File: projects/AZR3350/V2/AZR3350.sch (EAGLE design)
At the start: 168 parts, among them IC1 LM2734Y, IC11 74HC125, IC2 LDO-TS1117CW-3V3, IC3 74S08D, IC5 A4988, IC6 A4988, IC7 A4988, IC8 A4988, IC9 SI87XXIS, J107 ZX62-AB-5PA, Q1 FDS6890A, Q2 IRF520, Q3 IRF520, X3 MSTBV4

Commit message: Found all of the parts on DigiKey
(and replaced most that didn't work, for various reasons)
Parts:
- removed IC11: 74HC125, misc:74HC125
- removed L6: 10uH 100MHz, Zero_V1.0:INDUCTOR-0603
- removed R75: 4K7, resistor:R-US_R0603
- removed R76: 180R, resistor:R-US_R0603
- removed U$2: ATSAM4S8C, misc:ATSAM4S8C
- removed U$3: MICROSD, adafruit:MICROSD
- added 5V, USB: (no value), led:LEDCHIPLED_0805
- added C37, C38, C39, C41: 100n, resistor:C-EUC0603
- added C40, C42: 220n, resistor:C-EUC0603
- added F1: MC36207, misc:MC36207
- added IC10: A4988, RepRapjr:A4988
- added IC4: SI87XXIS, misc:SI87XXIS
- added J4: MOLEX-105162-001, misc:MOLEX-105162-001
- added J_ERASE: (no value), jumper:JP1Q
- added L3: 10uH 100MHz, Zero_V1.0:INDUCTOR-0603
- added Q4: BUK9Y53-100B, misc:BUK9Y53-100B
- added R62, R69: 100K, resistor:R-US_R0603
- added R63, R70: 10K, resistor:R-TRIMM3103
- added R64, R71: 20K, resistor:R-US_R0603
- added R65, R67: 10K, resistor:R-US_R0603
- added R66, R68: 0R2, resistor:R-US_R0805
- added RESET: PUSHBUTTON3, Zero_V1.0:PUSHBUTTON3
- added X1: 12MHz, misc:CRYSTAL-4PIN
- C1: value 10uF -> 10n; device resistor:CPOL-USD -> resistor:C-EUC0603
- C11, C16, C23: value 220n -> 100n
- C13, C20: value 100u -> 100n; device resistor:CPOL-USD -> resistor:C-EUC0603
- C15, C36: value 100n -> 2.2u
- C18, C32: value 220n -> 10u
- C19: value 100n -> 4u7
- C2: value 10n -> 10uF; device resistor:C-EUC0603 -> resistor:CPOL-USD
- C25, C9: value 220n -> 10u; device resistor:C-EUC0603 -> resistor:C-EUC0805
- C27: value 100u -> 2.2u 0.1-10ohm ESR; device resistor:CPOL-USD -> resistor:C-EUC0603
- C28: value 100n -> 10n
- C29: value 100n -> 10p
- C3: value 47u -> 100n; device resistor:CPOL-USD -> resistor:C-EUC0603
- C30: value 220n -> 10p
- C31: value 100n -> 10u
- C33: value 100n -> 2K2
- C34: value 100u -> 2.2u; device resistor:CPOL-USD -> resistor:C-EUC0603
- C4: value 4.7uF -> 47u; device resistor:C-EUC0603 -> resistor:CPOL-USD
- C43: value 2.2u -> 100n
- C44: value 2.2u -> 100u; device resistor:C-EUC0603 -> resistor:CPOL-USD
- C45, C46, C53, C55: value 10u -> 100n
- C47: value 2K2 -> 220n
- C49, C54, C56, C61, C63: value 100n -> 220n
- C5: value 10uF -> 4.7uF; device resistor:CPOL-USD -> resistor:C-EUC0603
- C51, C58: value 100n -> 100u; device resistor:C-EUC0603 -> resistor:CPOL-USD
- C57: value 4u7 -> 100n
- C6: value 4.7uF -> 10uF; device resistor:C-EUC0603 -> resistor:CPOL-USD
- C60: value 2.2u 0.1-10ohm ESR -> 100n
- C65: value 10u -> 100u; device resistor:C-EUC0603 -> resistor:CPOL-USD
- C7: value 100n -> 4.7uF
- D1: device Diodi:0012_CD1206-S01575 -> adafruit:DIODE_SOD-123FL
- D2: device Diodi:0012_CD1206-S01575 -> diode:DIODE-SOD123
- IC3: value 74S08D -> ATSAM4S8C; device 74xx-us:74S08D -> misc:ATSAM4S8C
- IC5: value A4988 -> 74HC125; device RepRapjr:A4988 -> misc:74HC125
- IC6: value A4988 -> 74S08D; device RepRapjr:A4988 -> 74xx-us:74S08D
- IC9: value SI87XXIS -> A4988; device misc:SI87XXIS -> RepRapjr:A4988
- Q1: value FDS6890A -> NX138BKS; device transistor-power:FDS6890A -> misc:NX138BKS
- R1: value 10k -> 47K
- R10: value 47R -> 27K
- R11: value 10K -> 47K
- R12, R14, R33: value 0R2 -> 10K; device resistor:R-US_R0805 -> resistor:R-US_R0603
- R13: value 10K -> 1R
- R15: value 100K -> 4K7
- R16: value 10K -> 470R; device resistor:R-TRIMM3103 -> resistor:R-US_R0603
- R17: value 20K -> 47R
- R18: value 10K -> 47R
- R19: value 0R2 -> 47R; device resistor:R-US_R0805 -> resistor:R-US_R0603
- R2: value 52.3k -> 4K7
- R20: value 10K -> 2K2
- R21: value 0R2 -> 2K2; device resistor:R-US_R0805 -> resistor:R-US_R0603
- R22: value 100K -> 470R
- R23: value 10K -> 2K2; device resistor:R-TRIMM3103 -> resistor:R-US_R0603
- R24: value 20K -> 2K2
- R25, R27: value 10K -> 220R
- R26: value 0R2 -> 220R; device resistor:R-US_R0805 -> resistor:R-US_R0603
- R28: value 0R2 -> 100R; device resistor:R-US_R0805 -> resistor:R-US_R0603
- R29: value 100K -> 220R
- R3: value 10k -> 100k
- R30: value 10K -> 220R; device resistor:R-TRIMM3103 -> resistor:R-US_R0603
- R31: value 20K -> 220R
- R34: value 10K -> 1K
- R35: value 0R2 -> 1K; device resistor:R-US_R0805 -> resistor:R-US_R0603
- R36: value 100K -> 180R
- R37: value 10K -> 180R; device resistor:R-TRIMM3103 -> resistor:R-US_R0603
- R38: value 20K -> 10K
- R39: value 4K7 0.1% -> 10K
- R4: value 10K -> 5.53k
- R40: value 47R -> 4K7 0.1%
- R41: value 2K2 -> 4K7 0.1%
- R42, R43: value 1K -> 4K7
- R44: value 180R -> 10K
- R45: value 180R -> 0R2; device resistor:R-US_R0603 -> resistor:R-US_R0805
- R46, R51: value 4K7 -> 10K
- R47: value 4K7 -> 0R2; device resistor:R-US_R0603 -> resistor:R-US_R0805
- R48: value 470R -> 100K
- R49: value 2K2 -> 10K; device resistor:R-US_R0603 -> resistor:R-TRIMM3103
- R5: value 10K -> 10k
- R50: value 2K2 -> 20K
- R52: value 220R -> 0R2; device resistor:R-US_R0603 -> resistor:R-US_R0805
- R53, R58: value 220R -> 10K
- R54: value 100R -> 0R2; device resistor:R-US_R0603 -> resistor:R-US_R0805
- R55: value 220R -> 100K
- R56: value 220R -> 10K; device resistor:R-US_R0603 -> resistor:R-TRIMM3103
- R57: value 220R -> 20K
- R59: value 10K -> 0R2; device resistor:R-US_R0603 -> resistor:R-US_R0805
- R6: value 4K7 0.1% -> 4K7
- R61: value 1R -> 0R2; device resistor:R-US_R0603 -> resistor:R-US_R0805
- R7: value 470R -> 2K2
- R8: value 2K2 -> 180R
- R9: value 47R -> 2K2
- renumbered D103 to D4, J107 to J1, X3 to J3
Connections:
- removed net EN: IC1.EN, R1.2
- removed net N$19: R58.2, R59.1, U$3.CARD_DETECT, U$3.CARD_DETECT1
- removed net N$33: R75.1, VIN.C
- removed net N$34: 3V3.C, R76.1
- new net 24V_LED: R6.1, VIN.C
- new net 3V3_LED: 3V3.C, R8.1
- new net 5V_LED: 5V.C, R7.1
- new net CARDDETECT: J4.CARD_DETECT, R25.2, R32.1
- new net ERASE: IC3.ERASE/PB12, J_ERASE.2
- new net PWR_FAIL_DET: C1.1, IC3.PC12/AD12, R1.1, R2.2
- new net SHDN: IC1.EN, R3.2
- new net USB_LED: R9.1, USB.C
- new net USB_PWR_MON: C8.2, IC3.PC11, R10.2, R11.1
- new net VSSA: C15.1, F1.1, R12.2, T_BED-2.S, T_EXT-2.S
- new net VSSA_MON: IC3.PA17/PGMD5/AD0, R12.1
- new net XIN: C29.1, IC3.PB9/PGMCK/XIN, X1.3
- new net XOUT: C30.1, IC3.PB8/XOUT, X1.1
- net +24V: now also C2.+, C39.2, C41.1, C43.1, C44.+, C46.2, C48.1, C50.1, C51.+, C53.2, C55.1, C57.1, C58.+, C60.2, C62.1, C64.1, C65.+, IC10.VBB1, IC10.VBB2, IC9.VBB1, IC9.VBB2, R3.1, R42.2; no longer C1.+, C10.1, C12.1, C13.+, C15.2, C17.1, C19.1, C20.+, C22.2, C24.1, C26.1, C27.+, C29.2, C31.1, C33.1, C34.+, C8.2, IC5.VBB1, IC5.VBB2, IC6.VBB1, IC6.VBB2, R1.1, R46.2
- net +3V3: now also C10.2, C11.2, C12.2, C13.2, C14.2, C16.1, C31.1, C33.1, C36.1, C42.1, C49.1, C56.1, C6.+, C63.1, C7.2, C9.2, IC10.MS1, IC10.MS2, IC10.MS3, IC10.VDD, IC3.VDDIN, IC3.VDDIO-27, IC3.VDDIO-50, IC3.VDDIO-69, IC3.VDDIO-91, IC3.VDDIO-98, IC4.VDD, IC5P.VCC, IC9.MS1, IC9.MS2, IC9.MS3, J4.VDD, J_ERASE.1, L3.2, R14.2, R32.2, R33.2, R46.2, R48.2, R50.2, R53.2, R55.2, R57.2, R62.2, R64.2, R67.2, R69.2, R71.2; no longer C11.1, C25.1, C35.1, C45.1, C46.1, C47.1, C48.2, C49.2, C5.+, C50.2, C51.2, C52.2, C53.2, C54.1, C55.1, C6.2, IC11P.VCC, IC5.MS1, IC5.MS2, IC5.MS3, IC5.VDD, IC6.MS1, IC6.MS2, IC6.MS3, IC6.VDD, L4.2, R13.2, R15.2, R17.2, R20.2, R22.2, R24.2, R27.2, R29.2, R31.2, R34.2, R36.2, R38.2, R59.2, U$2.VDDIN, U$2.VDDIO-27, U$2.VDDIO-50, U$2.VDDIO-69, U$2.VDDIO-91, U$2.VDDIO-98, U$3.VDD
- net +5V: now also 5V.A, C37.1, C4.+, C5.1, EXP_2-10.S, IC6P.VCC, R4.1; no longer C3.+, C36.1, C4.1, EXP_1-10.S, IC3P.VCC, R2.1
- net ADVREF: now also C17.1, IC3.ADVREF, L3.1, R40.2, R41.2; no longer C56.1, L4.1, R39.2, R6.2, U$2.ADVREF
- net BED: now also IC3.PA15/PGMD3, R37.1; no longer R45.1, U$2.PA15/PGMD3
- net BEEPER: now also EXP_2-1.S, IC3.PC22; no longer EXP_1-1.S, U$2.PC22
- net BOOST: now also C3.1; no longer C2.1
- net BTN_EN1: now also EXP_1-5.S, IC3.PC20; no longer EXP_2-5.S, U$2.PC20
- net BTN_EN2: now also EXP_1-3.S, IC3.TCK/SWCLK/PB7; no longer EXP_2-3.S, U$2.TCK/SWCLK/PB7
- net BTN_ENC: now also EXP_2-2.S, IC3.PC14; no longer EXP_1-2.S, U$2.PC14
- net CP1E: now also C59.1, IC10.CP1; no longer C28.1, IC8.CP1
- net CP1X: now also C38.1, IC7.CP1; no longer C7.1, IC5.CP1
- net CP1Y: now also C45.1, IC8.CP1; no longer C14.1, IC6.CP1
- net CP1Z: now also C52.1, IC9.CP1; no longer C21.1, IC7.CP1
- net CP2E: now also C59.2, IC10.CP2; no longer C28.2, IC8.CP2
- net CP2X: now also C38.2, IC7.CP2; no longer C7.2, IC5.CP2
- net CP2Y: now also C45.2, IC8.CP2; no longer C14.2, IC6.CP2
- net CP2Z: now also C52.2, IC9.CP2; no longer C21.2, IC7.CP2
- net EDR_CONN: now also R23.2; no longer R49.2
- net EMOT1A: now also IC10.OUT1A; no longer IC8.OUT1A
- net EMOT1B: now also IC10.OUT1B; no longer IC8.OUT1B
- net EMOT2A: now also IC10.OUT2A; no longer IC8.OUT2A
- net EMOT2B: now also IC10.OUT2B; no longer IC8.OUT2B
- net ESP_CS: now also R24.2; no longer R50.2
- net ESP_DATA_RDY: now also IC3.PC13/AD10, R23.1; no longer R49.1, U$2.PC13/AD10
- net ESP_EN: now also IC3.PA24/PGMD12, R15.1; no longer R51.1, U$2.PA24/PGMD12
- net ESP_MISO: now also R18.1; no longer R10.1
- net ESP_MOSI: now also R19.1; no longer R40.1
- net ESP_RESET: now also R16.2, R20.2; no longer R7.2, R8.2
- net ESP_RST: now also IC3.PC4, R16.1; no longer R7.1, U$2.PC4
- net ESP_SPCK: now also R17.1; no longer R9.1
- net ESP_URDX: now also R21.2; no longer R41.2
- net ESP_UTDX: now also R22.2; no longer R48.2
- net E_DIR: now also IC10.DIR, IC3.PC2; no longer IC8.DIR, U$2.PC2
- net E_EN: now also IC10.EN, IC3.PA8/XOUT32/PGMM0, R67.1; no longer IC8.EN, R34.1, U$2.PA8/XOUT32/PGMM0
- net E_STEP: now also IC10.STEP, IC3.PC1; no longer IC8.STEP, U$2.PC1
- net FAN1: now also IC3.PA18/PGMD6/AD1, R34.1; no longer R42.1, U$2.PA18/PGMD6/AD1
- net FAN2: now also IC3.PC26, R35.1; no longer R43.1, U$2.PC26
- net FB: now also R4.2, R5.1; no longer R2.2, R3.1
- net GND: now also C1.2, C10.1, C11.1, C12.1, C13.1, C14.1, C15.2, C2.-, C20.2, C21.2, C22.2, C27.2, C28.2, C29.2, C34.2, C37.2, C4.-, C40.2, C41.2, C42.2, C44.-, C48.2, C49.2, C5.2, C50.2, C51.-, C58.-, C6.-, C65.-, C7.1, C8.1, C9.1, F1.2, IC10.GND, IC10.GND1, IC10.NC, IC10.NC1, IC10.NC2, IC10.TH-PAD, IC3.GND-2, IC3.GND-26, IC3.GND-45, IC3.GND-70, IC3.GND-95, IC3.JTAGSEL, IC3.TST, IC4.C1, IC4.GND, IC5A.OE, IC5B.OE, IC5D.I, IC5D.OE, IC5P.GND, IC6A.I0, IC6A.I1, IC6P.GND, IC9.GND1, IC9.NC, IC9.NC1, IC9.NC2, IC9.TH-PAD, J4.GND, J4.VSS, R15.2, R2.1, R20.1, R44.2, R45.1, R47.1, R49.E, R5.2, R52.1, R54.1, R56.E, R58.2, R59.1, R6.2, R61.1, R63.E, R65.2, R66.1, R68.1, R7.2, R70.E, R8.2, R9.2, RESET.4, X1.2, X1.4; no longer C1.-, C10.2, C11.2, C12.2, C13.-, C20.-, C27.-, C3.-, C34.-, C4.2, C44.2, C45.2, C46.2, C48.1, C49.1, C5.-, C50.1, C51.1, C52.1, C53.1, C58.2, C59.2, C6.1, C60.2, C65.2, C9.2, IC11A.OE, IC11B.OE, IC11D.I, IC11D.OE, IC11P.GND, IC3A.I0, IC3A.I1, IC3P.GND, IC5.GND, IC5.GND1, IC5.NC, IC5.NC1, IC5.NC2, IC5.TH-PAD, IC6.GND, IC6.GND1, IC6.NC, IC6.NC1, IC6.NC2, IC6.TH-PAD, IC9.C1, R12.1, R14.1, R16.E, R18.2, R19.1, R21.1, R23.E, R25.2, R26.1, R28.1, R3.2, R30.E, R32.2, R33.1, R35.1, R37.E, R75.2, R76.2, R8.1, T_BED-2.S, T_EXT-2.S, U$2.GND-2, U$2.GND-26, U$2.GND-45, U$2.GND-70, U$2.GND-95, U$2.TST, U$3.GND, U$3.GND1, U$3.VSS
- net HOTEND: now also IC3.PC3, R36.1; no longer R44.1, U$2.PC3
- net LCD_CS: now also IC3.PC19, IC6B.I0, IC6B.I1, IC6C.I1, IC6D.I1; no longer IC3B.I0, IC3B.I1, IC3C.I1, IC3D.I1, U$2.PC19
- net LCD_CS_BUF: now also EXP_2-4.S, IC6B.O; no longer EXP_1-4.S, IC3B.O
- net LCD_MISO: now also IC3.PA5/PGMRDY, IC5C.O; no longer IC11C.O, U$2.PA5/PGMRDY
- net LCD_MISO_BUF: now also EXP_1-1.S, IC5C.I; no longer EXP_2-1.S, IC11C.I
- net LCD_MOSI: now also IC3.PB6/PGMNOE, IC5A.I, IC6C.I0; no longer IC11A.I, IC3C.I0, U$2.PB6/PGMNOE
- net LCD_MOSI_BUF: now also EXP_2-3.S, IC6C.O; no longer EXP_1-3.S, IC3C.O
- net LCD_RST: now also EXP_1-8.S, IC3.PC21; no longer EXP_2-8.S, U$2.PC21
- net LCD_SCK: now also IC3.PA2/PGMEN2, IC5B.I, IC6D.I0; no longer IC11B.I, IC3D.I0, U$2.PA2/PGMEN2
- net LCD_SCK_BUF: now also EXP_2-5.S, IC6D.O; no longer EXP_1-5.S, IC3D.O
- net LCD_SD_CS: now also EXP_1-4.S, IC3.PB13/DAC0, IC5C.OE; no longer EXP_2-4.S, IC11C.OE, U$2.PB13/DAC0
- net MCCDA: now also IC3.PA28, R27.1; no longer R53.1, U$2.PA28
- net MCCK: now also IC3.PA29, R28.1; no longer R54.1, U$2.PA29
- net MCDA0: now also IC3.PA30, R26.1; no longer R52.1, U$2.PA30
- net MCDA1: now also IC3.PA31, R30.1; no longer R56.1, U$2.PA31
- net MCDA2: now also IC3.PA26/PGMD14, R31.1; no longer R57.1, U$2.PA26/PGMD14
- net MCDA3: now also IC3.PA27/PGMD15, R29.1; no longer R55.1, U$2.PA27/PGMD15
- net MISO: now also IC3.PA12/PGMD0, R18.2; no longer R10.2, U$2.PA12/PGMD0
- net MOSI: now also IC3.PA13/PGMD1, R19.2; no longer R40.2, U$2.PA13/PGMD1
- net N$13: now also R34.2; no longer R42.2
- net N$18: now also R35.2; no longer R43.2
- net N$20: now also R36.2; no longer R44.2
- net N$25: now also R37.2; no longer R45.2
- net N$26: now also R42.1; no longer R46.1
- net N$27: now also R43.1; no longer R47.1
- net N$28: now also J4.DAT0, R26.2; no longer R52.2, U$3.DATA_OUT
- net N$29: now also J4.CMD, R27.2, R33.1; no longer R53.2, R60.1, U$3.DATA_IN
- net N$30: now also J4.CLK, R28.2; no longer R54.2, U$3.SCLK
- net N$31: now also J4.DAT3, R29.2; no longer R55.2, U$3.CS
- net N$32: now also J4.DAT1, R30.2; no longer R56.2, U$3.DAT1
- net N$35: now also J4.DAT2, R31.2; no longer R57.2, U$3.DAT2
- net N$37: now also C19.1, R13.1; no longer C57.1, R61.1
- net NPCS0: now also IC3.PA11/PGMM3, R24.1; no longer R50.1, U$2.PA11/PGMM3
- net NRST: now also C28.1, IC3.NRST, R14.1, RESET.2; no longer U$2.NRST
- net REFE: now also IC10.REF, R70.S; no longer IC8.REF, R37.S
- net REFE-IN: now also R70.A, R71.1; no longer R37.A, R38.1
- net REFX: now also IC7.REF, R49.S; no longer IC5.REF, R16.S
- net REFX-IN: now also R49.A, R50.1; no longer R16.A, R17.1
- net REFY: now also IC8.REF, R56.S; no longer IC6.REF, R23.S
- net REFY-IN: now also R56.A, R57.1; no longer R23.A, R24.1
- net REFZ: now also IC9.REF, R63.S; no longer IC7.REF, R30.S
- net REFZ-IN: now also R63.A, R64.1; no longer R30.A, R31.1
- net ROSCE: now also IC10.ROSC, R65.1; no longer IC8.ROSC, R32.1
- net ROSCX: now also IC7.ROSC, R44.1; no longer IC5.ROSC, R11.1
- net ROSCY: now also IC8.ROSC, R51.1; no longer IC6.ROSC, R18.1
- net ROSCZ: now also IC9.ROSC, R58.1; no longer IC7.ROSC, R25.1
- net RSTE: now also IC10.RST, IC10.SLP, R69.1; no longer IC8.RST, IC8.SLP, R36.1
- net RSTX: now also IC7.RST, IC7.SLP, R48.1; no longer IC5.RST, IC5.SLP, R15.1
- net RSTY: now also IC8.RST, IC8.SLP, R55.1; no longer IC6.RST, IC6.SLP, R22.1
- net RSTZ: now also IC9.RST, IC9.SLP, R62.1; no longer IC7.RST, IC7.SLP, R29.1
- net SAM_TFR_RDY: now also IC3.PA23/PGMD11; no longer U$2.PA23/PGMD11
- net SD_CD: now also IC3.PC8, R25.1; no longer R58.1, U$2.PC8
- net SD_MOSI_BUF: now also EXP_1-6.S, IC5A.O; no longer EXP_2-6.S, IC11A.O
- net SD_SCK_BUF: now also EXP_1-2.S, IC5B.O; no longer EXP_2-2.S, IC11B.O
- net SNS1E: now also IC10.SNS1, R66.2; no longer IC8.SNS1, R33.2
- net SNS1X: now also IC7.SNS1, R45.2; no longer IC5.SNS1, R12.2
- net SNS1Y: now also IC8.SNS1, R52.2; no longer IC6.SNS1, R19.2
- net SNS1Z: now also IC9.SNS1, R59.2; no longer IC7.SNS1, R26.2
- net SNS2E: now also IC10.SNS2, R68.2; no longer IC8.SNS2, R35.2
- net SNS2X: now also IC7.SNS2, R47.2; no longer IC5.SNS2, R14.2
- net SNS2Y: now also IC8.SNS2, R54.2; no longer IC6.SNS2, R21.2
- net SNS2Z: now also IC9.SNS2, R61.2; no longer IC7.SNS2, R28.2
- net SPCK: now also IC3.PA14/PGMD2, R17.2; no longer R9.2, U$2.PA14/PGMD2
- net SW: now also C3.2; no longer C2.2
- net T_BED: now also C35.1, IC3.PB1/AD5, R38.1; no longer C43.1, R4.1, U$2.PB1/AD5
- net T_BED_IN: now also R38.2, R41.1; no longer R4.2, R6.1
- net T_EXT: now also C34.1, IC3.PB0/AD4, R39.1; no longer C44.1, R5.1, U$2.PB0/AD4
- net T_EXT_IN: now also R39.2, R40.1; no longer R39.1, R5.2
- net URXD1: now also IC3.PB2/AD6, R21.1; no longer R41.1, U$2.PB2/AD6
- net USB_N: now also IC3.DDM/PB10; no longer U$2.DDM/PB10
- net USB_P: now also IC3.DDP/PB11; no longer U$2.DDP/PB11
- net UTXD1: now also IC3.PB3/AD7, R22.1; no longer R48.1, U$2.PB3/AD7
- net VBUS: now also R10.1, USB.A
- net VCPE: now also C60.1, IC10.VCP; no longer C29.1, IC8.VCP
- net VCPX: now also C39.1, IC7.VCP; no longer C8.1, IC5.VCP
- net VCPY: now also C46.1, IC8.VCP; no longer C15.1, IC6.VCP
- net VCPZ: now also C53.1, IC9.VCP; no longer C22.1, IC7.VCP
- net VDDOUT: now also C21.1, C22.1, C23.1, C24.1, C25.1, C26.1, C27.1, IC3.VDDCORE-16, IC3.VDDCORE-36, IC3.VDDCORE-56, IC3.VDDCORE-85, IC3.VDDOUT, L4.2; no longer C59.1, C60.1, C61.1, C62.1, C63.1, C64.1, C65.1, L6.2, U$2.VDDCORE-16, U$2.VDDCORE-36, U$2.VDDCORE-56, U$2.VDDCORE-85, U$2.VDDOUT
- net VDDPLL: now also C20.1, IC3.VDDPLL, L4.1, R13.2; no longer C58.1, L6.1, R61.2, U$2.VDDPLL
- net VIN: now also R1.2, R43.2; no longer R47.2
- net VREGE: now also C61.1, IC10.VREG; no longer C30.1, IC8.VREG
- net VREGX: now also C40.1, IC7.VREG; no longer C9.1, IC5.VREG
- net VREGY: now also C47.1, IC8.VREG; no longer C16.1, IC6.VREG
- net VREGZ: now also C54.1, IC9.VREG; no longer C23.1, IC7.VREG
- net XMOT1A: now also IC7.OUT1A; no longer IC5.OUT1A
- net XMOT1B: now also IC7.OUT1B; no longer IC5.OUT1B
- net XMOT2A: now also IC7.OUT2A; no longer IC5.OUT2A
- net XMOT2B: now also IC7.OUT2B; no longer IC5.OUT2B
- net X_DIR: now also IC3.PA1/PGMEN1, IC7.DIR; no longer IC5.DIR, U$2.PA1/PGMEN1
- net X_EN: now also IC3.PC17, IC7.EN, R46.1; no longer IC5.EN, R13.1, U$2.PC17
- net X_STEP: now also IC3.PC16, IC7.STEP; no longer IC5.STEP, U$2.PC16
- net X_STOP: now also IC3.TMS/SWDIO/PB6; no longer U$2.TMS/SWDIO/PB6
- net YMOT1A: now also IC8.OUT1A; no longer IC6.OUT1A
- net YMOT1B: now also IC8.OUT1B; no longer IC6.OUT1B
- net YMOT2A: now also IC8.OUT2A; no longer IC6.OUT2A
- net YMOT2B: now also IC8.OUT2B; no longer IC6.OUT2B
- net Y_DIR: now also IC3.PC9, IC8.DIR; no longer IC6.DIR, U$2.PC9
- net Y_EN: now also IC3.PA3, IC8.EN, R53.1; no longer IC6.EN, R20.1, U$2.PA3
- net Y_STEP: now also IC3.PC10, IC8.STEP; no longer IC6.STEP, U$2.PC10
- net Y_STOP: now also IC3.PC18; no longer U$2.PC18
- net ZMOT1A: now also IC9.OUT1A; no longer IC7.OUT1A
- net ZMOT1B: now also IC9.OUT1B; no longer IC7.OUT1B
- net ZMOT2A: now also IC9.OUT2A; no longer IC7.OUT2A
- net ZMOT2B: now also IC9.OUT2B; no longer IC7.OUT2B
- net Z_DIR: now also IC3.TDI/PB4, IC9.DIR; no longer IC7.DIR, U$2.TDI/PB4
- net Z_EN: now also IC3.PA4/PGMNCMD, IC9.EN, R60.1; no longer IC7.EN, R27.1, U$2.PA4/PGMNCMD
- net Z_STEP: now also IC3.PC28, IC9.STEP; no longer IC7.STEP, U$2.PC28
- net Z_STOP: now also IC3.TDO/TRACESWO/PB5, IC4.OUT; no longer IC9.OUT, U$2.TDO/TRACESWO/PB5
- net Z_STOP_IN: now also IC4.A1; no longer IC9.A1
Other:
- moved on the sheet: 3V3, C10, C11, C12, C14, C15, C16, C17, C18, C19, C21, C22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

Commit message: Changed out mosfets, other improvements (APSR)
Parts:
- removed Q4: BUK9Y53-100B, misc:BUK9Y53-100B
- Q2, Q3: value IRF520 -> BUK9Y53-100B; device transistor-power:IRF520 -> misc:BUK9Y53-100B
- RESET: value PUSHBUTTON3 -> (none); device Zero_V1.0:PUSHBUTTON3 -> misc:EVQQ2
- renumbered J_ERASE to ERASE
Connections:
- net CARDDETECT renamed DET
- net N$1 renamed VIN_F
- net N$10 renamed ESP_VIN
- net N$13 renamed FAN1_G
- net N$18 renamed FAN2_G
- net N$20 renamed EXT_G
- net N$21 renamed FAN2_D
- net N$22 renamed FAN1_D
- net N$23 renamed EXT_D
- net N$24 renamed BED_D
- net N$25 renamed BED_G
- net N$26 renamed EXT_L
- net N$27 renamed BED_L
- net N$28 renamed DAT0
- net N$29 renamed CMD
- net N$30 renamed CLK
- net N$31 renamed DAT3
- net N$32 renamed DAT1
- net N$35 renamed DAT2
- removed net NRST: C28.1, IC3.NRST, R14.1, RESET.2
- new net RESET: C28.1, IC3.NRST, R14.1, RESET.P1
- net GND: now also RESET.S, RESET.S1; no longer RESET.4

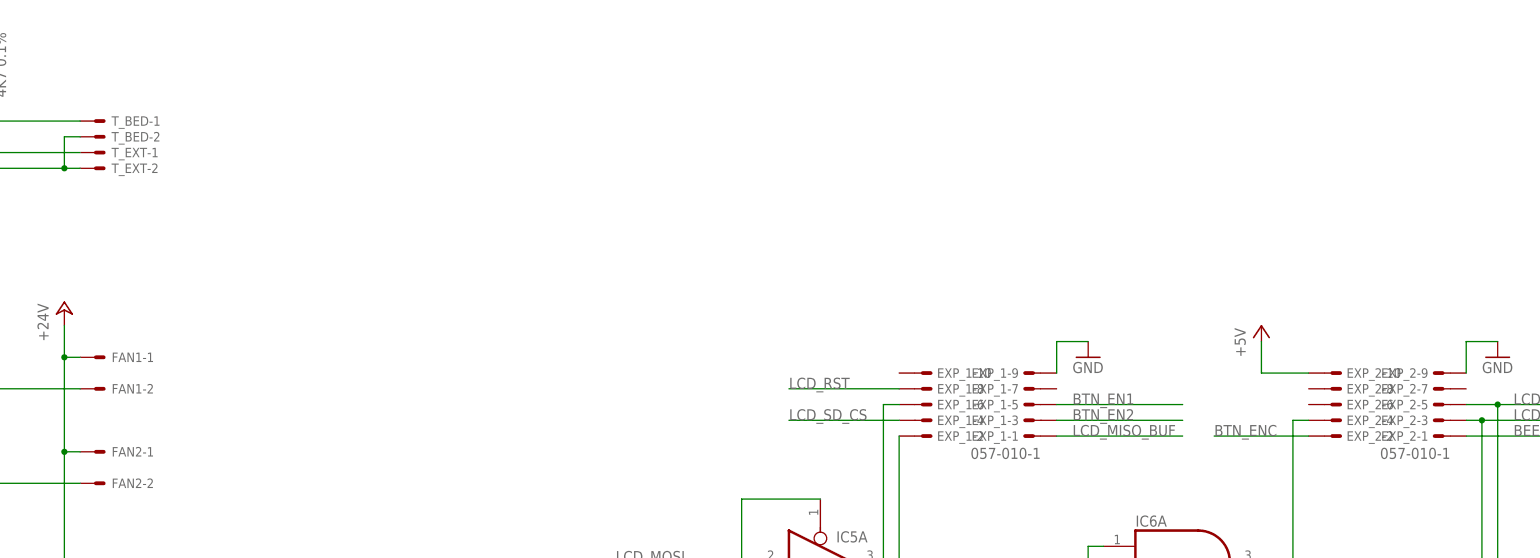
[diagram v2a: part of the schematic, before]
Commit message: LCD screen
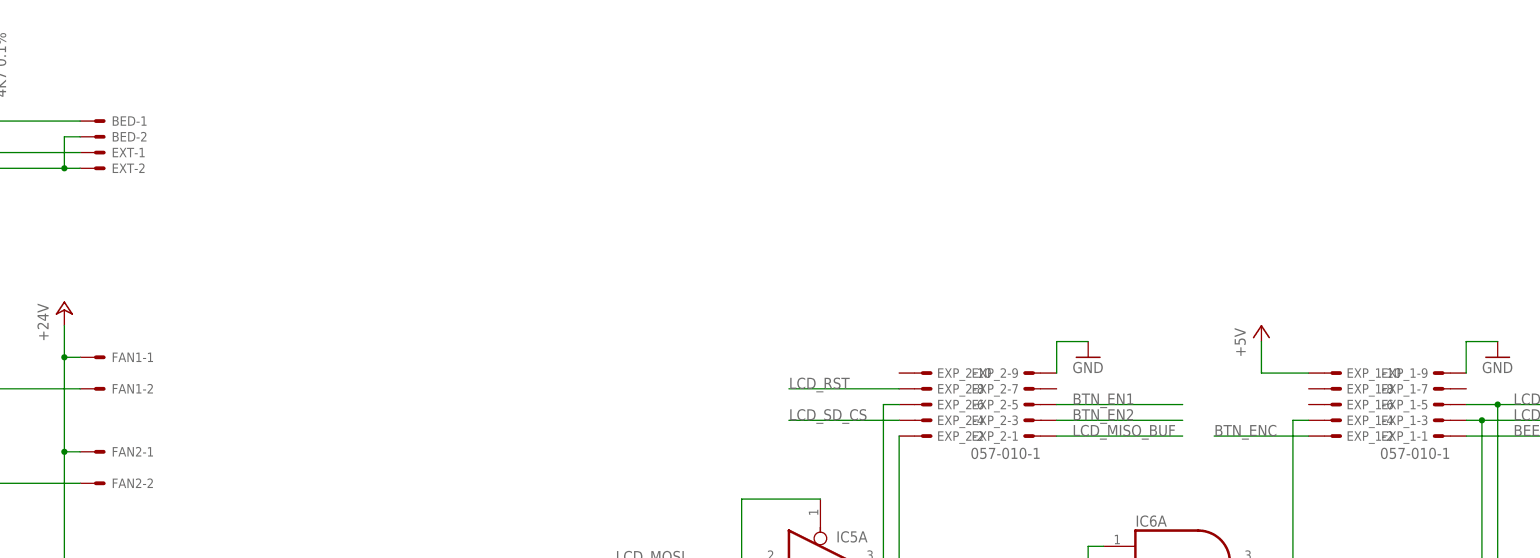
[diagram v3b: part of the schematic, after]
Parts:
- renumbered T_BED to BED, T_EXT to EXT
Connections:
- net +5V: now also EXP_1-10.S; no longer EXP_2-10.S
- net BEEPER: now also EXP_1-1.S; no longer EXP_2-1.S
- net BTN_EN1: now also EXP_2-5.S; no longer EXP_1-5.S
- net BTN_EN2: now also EXP_2-3.S; no longer EXP_1-3.S
- net BTN_ENC: now also EXP_1-2.S; no longer EXP_2-2.S
- net LCD_CS_BUF: now also EXP_1-4.S; no longer EXP_2-4.S
- net LCD_MISO_BUF: now also EXP_2-1.S; no longer EXP_1-1.S
- net LCD_MOSI_BUF: now also EXP_1-3.S; no longer EXP_2-3.S
- net LCD_RST: now also EXP_2-8.S; no longer EXP_1-8.S
- net LCD_SCK_BUF: now also EXP_1-5.S; no longer EXP_2-5.S
- net LCD_SD_CS: now also EXP_2-4.S; no longer EXP_1-4.S
- net SD_MOSI_BUF: now also EXP_2-6.S; no longer EXP_1-6.S
- net SD_SCK_BUF: now also EXP_2-2.S; no longer EXP_1-2.S
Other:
- moved on the sheet: EXP_1-1, EXP_1-10, EXP_1-2, EXP_1-3, EXP_1-4, EXP_1-5, EXP_1-6, EXP_1-7, EXP_1-8, EXP_1-9, EXP_2-1, EXP_2-10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
